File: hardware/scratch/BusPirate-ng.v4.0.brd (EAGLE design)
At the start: 80 x 49 mm, 145 parts, among them CON1 CON-USB-F-MICRO-B, IC1 IC_UC_STM32F103RBTXX-LQFP64, IC10 74LVC1G07DBV, IC11 IC_BUFF_SN74LVC1T45DBV, IC12 74LVC1G07DBV, IC13 IC_BUFF_SN74LVC1T45DBV, IC14 74LVC1G07DBV, IC15 IC_BUFF_SN74LVC1T45DBV, IC16 74LVC1G07DBV, IC17 IC_BUFF_SN74LVC1T45DBV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

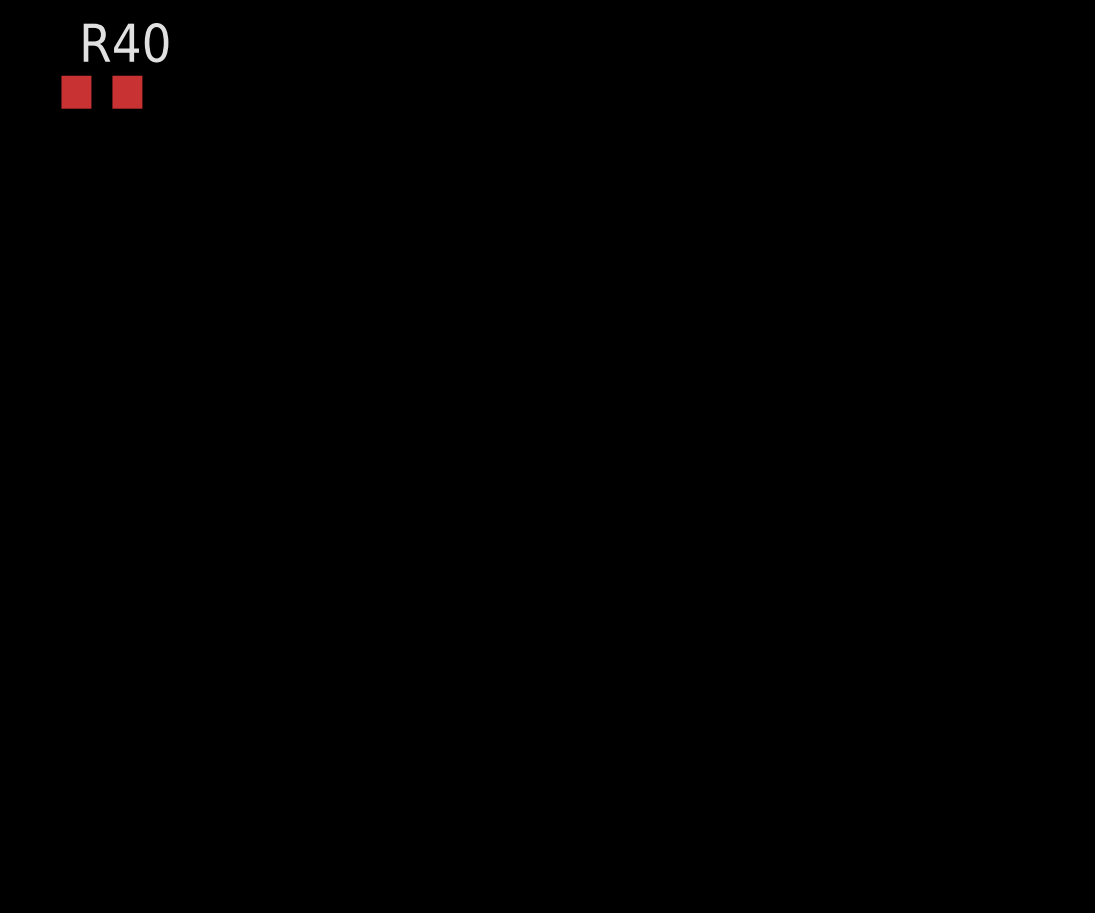
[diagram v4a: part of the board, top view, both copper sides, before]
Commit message: wired: -IO headers -CRESET -CDONE -MCU_MCO (Master Clock Out) to FPGA -FPGA to IO buffers -VCCPLL with 0.1uF cap and GNDPLL -2 interrupts from FPGA but not yet connected
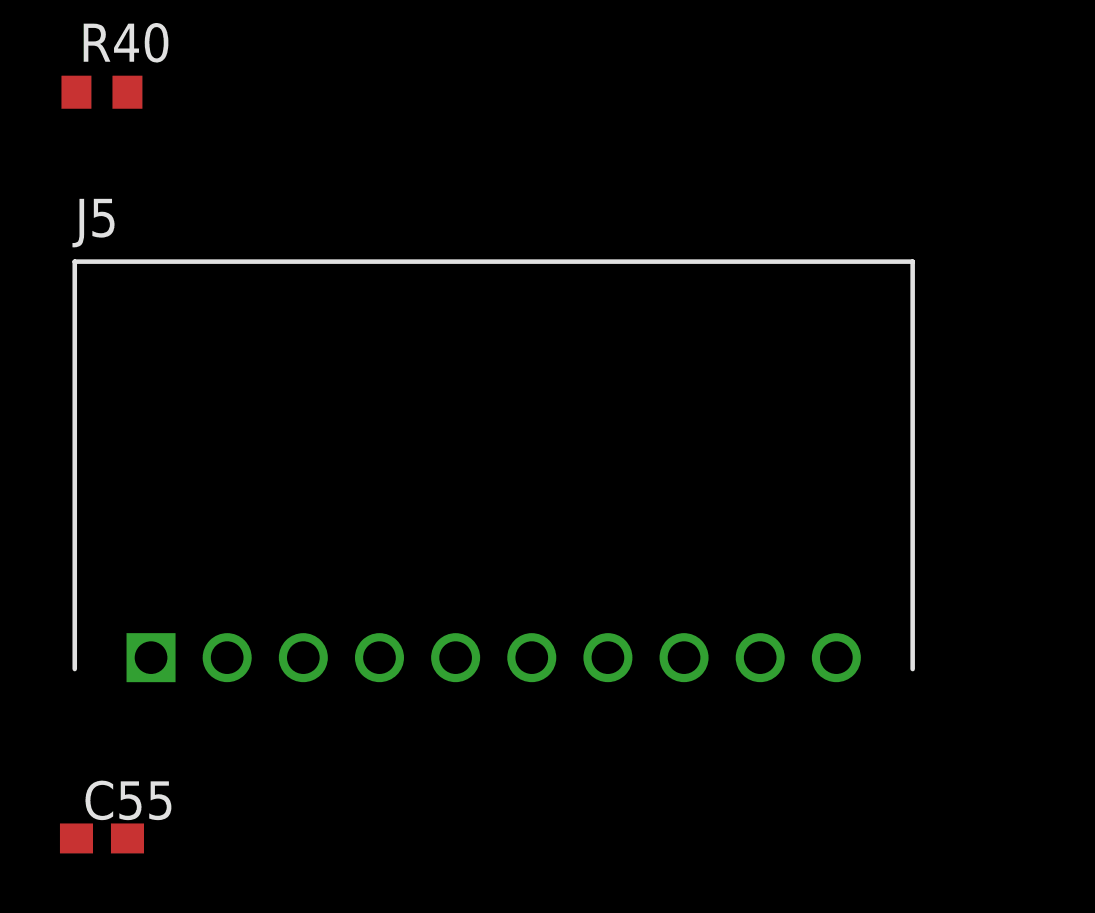
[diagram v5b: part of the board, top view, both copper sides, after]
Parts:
- added C55: 0.1uF, rcl:C0603
- added J5: CON_HEADER_1X10-RIGHT_ANGLED_PTH_SHROUDED, dp_devices.v6:M1X10_MALE_RIGHT_ANGLES_PTH_SHROUDED
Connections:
- removed net GNDPLL0: U1.53
- removed net GNDPLL1: U1.127
- removed net N$11: U1.3
- removed net N$12: R38.1, U1.66
- removed net N$14: R39.1, U1.65
- removed net VCCPLL0: U1.54
- new net FPGA_CDONE: R39.1, U1.65, U2.70
- new net FPGA_CRESET: R38.1, U1.66, U2.69
- new net MCU_INT0: U1.52
- new net MCU_INT1: U1.49
- new net MCU_MCO: U1.20, U2.100
- new net N$10: U2.56
- new net N$23: U1.110
- new net N$24: U1.129
- new net N$25: U1.128
- net 1V2: now also C55.2, U1.54
- net BPIO_AUX: now also J5.6
- net BPIO_CLOCK: now also J5.9
- net BPIO_CS: now also J5.7
- net BPIO_MISO: now also J5.8
- net BPIO_MOSI: now also J5.10
- net BUFDIR_AUX: now also U1.95
- net BUFDIR_CLOCK: now also U1.104
- net BUFDIR_CS: now also U1.91
- net BUFDIR_MISO: now also U1.99
- net BUFDIR_MOSI: now also U1.107
- net BUFIO_AUX: now also U1.94
- net BUFIO_CLOCK: now also U1.102
- net BUFIO_CS: now also U1.90
- net BUFIO_MISO: now also U1.98
- net BUFIO_MOSI: now also U1.106
- net BUFOD_AUX: now also U1.93
- net BUFOD_CLOCK: now also U1.101
- net BUFOD_CS: now also U1.88
- net BUFOD_MISO: now also U1.97
- net BUFOD_MOSI: now also U1.105
- net FSMC_A0: now also U1.3; no longer U1.10
- net FSMC_A1: now also U1.4; no longer U1.11
- net FSMC_A2: now also U1.7; no longer U1.12
- net FSMC_A3: now also U1.8; no longer U1.15
- net FSMC_A4: now also U1.9; no longer U1.16
- net FSMC_A5: now also U1.10; no longer U1.17
- net FSMC_D4: now also U1.15; no longer U1.18
- net FSMC_D5: now also U1.16; no longer U1.19
- net FSMC_D6: now also U1.17; no longer U1.20
- net FSMC_D7: now also U1.18; no longer U1.21
- net FSMC_D8: now also U1.19; no longer U1.22
- net GND: now also C55.1, J5.1, U1.127, U1.53
- net IO_ADC/DAC: now also J5.5
- net N$15: now also U1.11; no longer U1.4
- net N$19: now also U1.12; no longer U1.7
- net N$21: now also U1.21; no longer U1.8
- net N$22: now also U1.22; no longer U1.9
- net SWV33: now also J5.3
- net SWV50: now also J5.2
- net VEXTERN: now also J5.4
